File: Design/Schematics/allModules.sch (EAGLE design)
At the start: 188 parts, among them IC1 MAX7219CNG, IC2 MAX7219CNG, IC3 MAX7219CNG, IC4 MAX7219CNG, SW1 arcade_btn, SW2 arcade_btn, SW3 arcade_btn, SW4 arcade_btn, U1 328P, U2 328P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

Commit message: Updated memory schematic to I2C
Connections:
- new net PB5: R37.1, U6.PB5(SCK)
- new net SCL: U6.PC5(ADC5/SCL)
- new net SDA: U6.PC4(ADC4/SDA)
- net N$114: now also U6.PC3(ADC3); no longer R37.1, U6.PC2(ADC2), U6.PC4(ADC4/SDA)
- net N$134: now also U6.PC2(ADC2); no longer U6.PC3(ADC3)
- net NICS_RX: no longer U6.PB0(ICP)
- net NICS_TX: no longer U6.PB1(OC1A)
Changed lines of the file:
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@@
 <net name="N$114" class="0">
 <segment>
-<wire x1="-45.72" y1="-48.26" x2="-45.72" y2="-10.16" width="0.1524" layer="91"/>
+<wire x1="-45.72" y1="-48.26" x2="-45.72" y2="-12.7" width="0.1524" layer="91"/>
 <pinref part="R38" gate="G$1" pin="1"/>
-<pinref part="U6" gate="G$1" pin="PC4(ADC4/SDA)"/>
-<wire x1="-58.42" y1="-10.16" x2="-45.72" y2="-10.16" width="0.1524" layer="91"/>
-</segment>
-<segment>
-<wire x1="-53.34" y1="-40.64" x2="-53.34" y2="-17.78" width="0.1524" layer="91"/>
+<pinref part="U6" gate="G$1" pin="PC3(ADC3)"/>
+<wire x1="-45.72" y1="-12.7" x2="-58.42" y2="-12.7" width="0.1524" layer="91"/>
+</segment>
+<segment>
+<wire x1="-53.34" y1="-40.64" x2="-53.34" y2="-20.32" width="0.1524" layer="91"/>
 <wire x1="-53.34" y1="-40.64" x2="-76.2" y2="-40.64" width="0.1524" layer="91"/>
 <wire x1="-76.2" y1="-40.64" x2="-76.2" y2="-48.26" width="0.1524" layer="91"/>
 <pinref part="R36" gate="G$1" pin="1"/>
-<pinref part="U6" gate="G$1" pin="PC1(ADC1)"/>
-<wire x1="-53.34" y1="-17.78" x2="-58.42" y2="-17.78" width="0.1524" layer="91"/>
-</segment>
-<segment>
-<wire x1="-55.88" y1="-38.1" x2="-55.88" y2="-20.32" width="0.1524" layer="91"/>
-<wire x1="-88.9" y1="-38.1" x2="-55.88" y2="-38.1" width="0.1524" layer="91"/>
-<wire x1="-88.9" y1="-48.26" x2="-88.9" y2="-38.1" width="0.1524" layer="91"/>
-<pinref part="R37" gate="G$1" pin="1"/>
 <pinref part="U6" gate="G$1" pin="PC0(ADC0)"/>
-<wire x1="-58.42" y1="-20.32" x2="-55.88" y2="-20.32" width="0.1524" layer="91"/>
+<wire x1="-58.42" y1="-20.32" x2="-53.34" y2="-20.32" width="0.1524" layer="91"/>
 </segment>
 <segment>
 <wire x1="-66.04" y1="-48.26" x2="-66.04" y2="-43.18" width="0.1524" layer="91"/>
 <wire x1="-66.04" y1="-43.18" x2="-50.8" y2="-43.18" width="0.1524" layer="91"/>
-<wire x1="-50.8" y1="-43.18" x2="-50.8" y2="-15.24" width="0.1524" layer="91"/>
+<wire x1="-50.8" y1="-43.18" x2="-50.8" y2="-17.78" width="0.1524" layer="91"/>
 <pinref part="R35" gate="G$1" pin="1"/>
-<pinref part="U6" gate="G$1" pin="PC2(ADC2)"/>
-<wire x1="-58.42" y1="-15.24" x2="-50.8" y2="-15.24" width="0.1524" layer="91"/>
+<pinref part="U6" gate="G$1" pin="PC1(ADC1)"/>
+<wire x1="-50.8" y1="-17.78" x2="-58.42" y2="-17.78" width="0.1524" layer="91"/>
 </segment>
 </net>
@@
 <net name="N$134" class="0">
 <segment>
-<wire x1="-48.26" y1="-45.72" x2="-48.26" y2="-12.7" width="0.1524" layer="91"/>
+<wire x1="-48.26" y1="-45.72" x2="-48.26" y2="-15.24" width="0.1524" layer="91"/>
 <wire x1="-48.26" y1="-45.72" x2="-55.88" y2="-45.72" width="0.1524" layer="91"/>
 <wire x1="-55.88" y1="-45.72" x2="-55.88" y2="-48.26" width="0.1524" layer="91"/>
 <pinref part="R34" gate="G$1" pin="1"/>
-<pinref part="U6" gate="G$1" pin="PC3(ADC3)"/>
-<wire x1="-48.26" y1="-12.7" x2="-58.42" y2="-12.7" width="0.1524" layer="91"/>
+<pinref part="U6" gate="G$1" pin="PC2(ADC2)"/>
+<wire x1="-58.42" y1="-15.24" x2="-48.26" y2="-15.24" width="0.1524" layer="91"/>
 </segment>
 </net>
@@
 </segment>
 </net>
-<net name="NICS_RX" class="0">
-<segment>
-<pinref part="U6" gate="G$1" pin="PB0(ICP)"/>
-<wire x1="-58.42" y1="25.4" x2="-55.88" y2="25.4" width="0.1524" layer="91"/>
-<label x="-55.88" y="25.4" size="1.778" layer="95" rot="MR180"/>
-</segment>
-</net>
-<net name="NICS_TX" class="0">
-<segment>
-<pinref part="U6" gate="G$1" pin="PB1(OC1A)"/>
-<wire x1="-58.42" y1="27.94" x2="-48.26" y2="27.94" width="0.1524" layer="91"/>
-<label x="-48.26" y="27.94" size="1.778" layer="95" rot="MR180"/>
-</segment>
-</net>
 <net name="MEM_RX" class="0">
 <segment>
 <pinref part="U6" gate="G$1" pin="PD0(RXD)"/>
-<wire x1="-58.42" y1="2.54" x2="-53.34" y2="2.54" width="0.1524" layer="91"/>
-<label x="-53.34" y="2.54" size="1.778" layer="95" rot="MR270"/>
+<wire x1="-58.42" y1="2.54" x2="-48.26" y2="2.54" width="0.1524" layer="91"/>
+<label x="-48.26" y="2.54" size="1.778" layer="95" rot="R270"/>
 </segment>
 <segment>
@@
 <pinref part="U6" gate="G$1" pin="PD1(TXD)"/>
 <wire x1="-58.42" y1="5.08" x2="-45.72" y2="5.08" width="0.1524" layer="91"/>
-<label x="-45.72" y="5.08" size="1.778" layer="95" rot="MR270"/>
+<label x="-45.72" y="5.08" size="1.778" layer="95" rot="R270"/>
 </segment>
 <segment>
@@
 </segment>
 </net>
+<net name="PB5" class="0">
+<segment>
+<pinref part="U6" gate="G$1" pin="PB5(SCK)"/>
+<wire x1="-58.42" y1="38.1" x2="-55.88" y2="38.1" width="0.1524" layer="91"/>
+<label x="-55.88" y="38.1" size="1.778" layer="95"/>
+</segment>
+<segment>
+<wire x1="-88.9" y1="-48.26" x2="-88.9" y2="-38.1" width="0.1524" layer="91"/>
+<pinref part="R37" gate="G$1" pin="1"/>
+<label x="-88.9" y="-38.1" size="1.778" layer="95"/>
+</segment>
+</net>
+<net name="SCL" class="0">
+<segment>
+<pinref part="U6" gate="G$1" pin="PC5(ADC5/SCL)"/>
+<wire x1="-58.42" y1="-7.62" x2="-55.88" y2="-7.62" width="0.1524" layer="91"/>
+<label x="-55.88" y="-7.62" size="1.778" layer="95" rot="MR180"/>
+</segment>
+</net>
+<net name="SDA" class="0">
+<segment>
+<pinref part="U6" gate="G$1" pin="PC4(ADC4/SDA)"/>
+<wire x1="-58.42" y1="-10.16" x2="-53.34" y2="-10.16" width="0.1524" layer="91"/>
+<label x="-53.34" y="-10.16" size="1.778" layer="95" rot="MR180"/>
+</segment>
+</net>

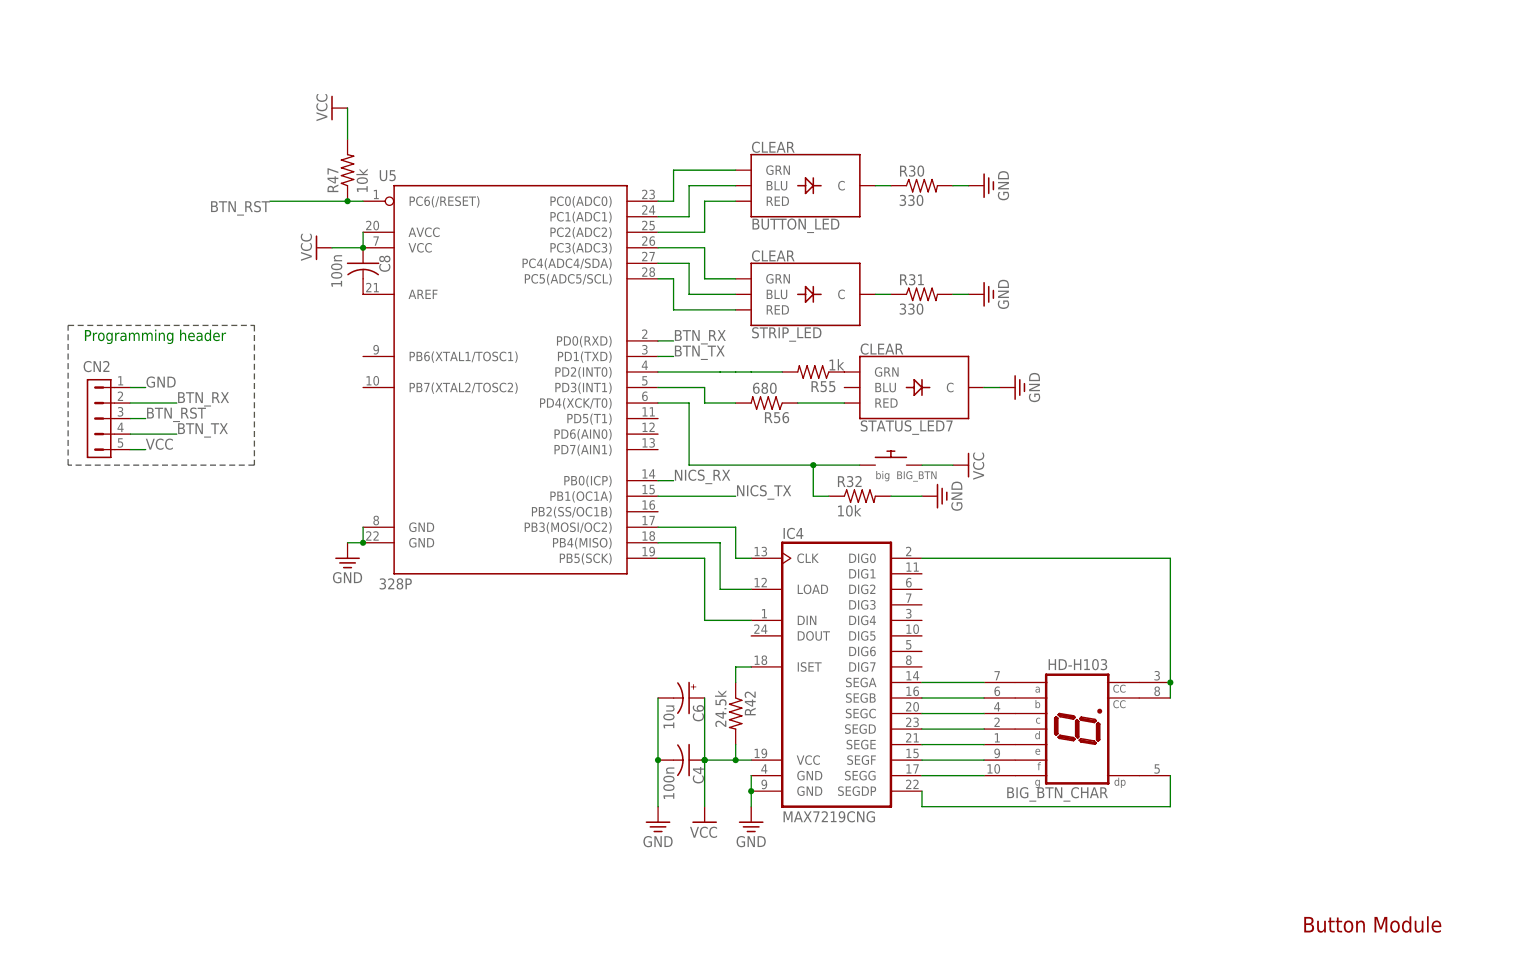
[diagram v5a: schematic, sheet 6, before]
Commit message: Updated modules for I2C and added external ADC for wires module
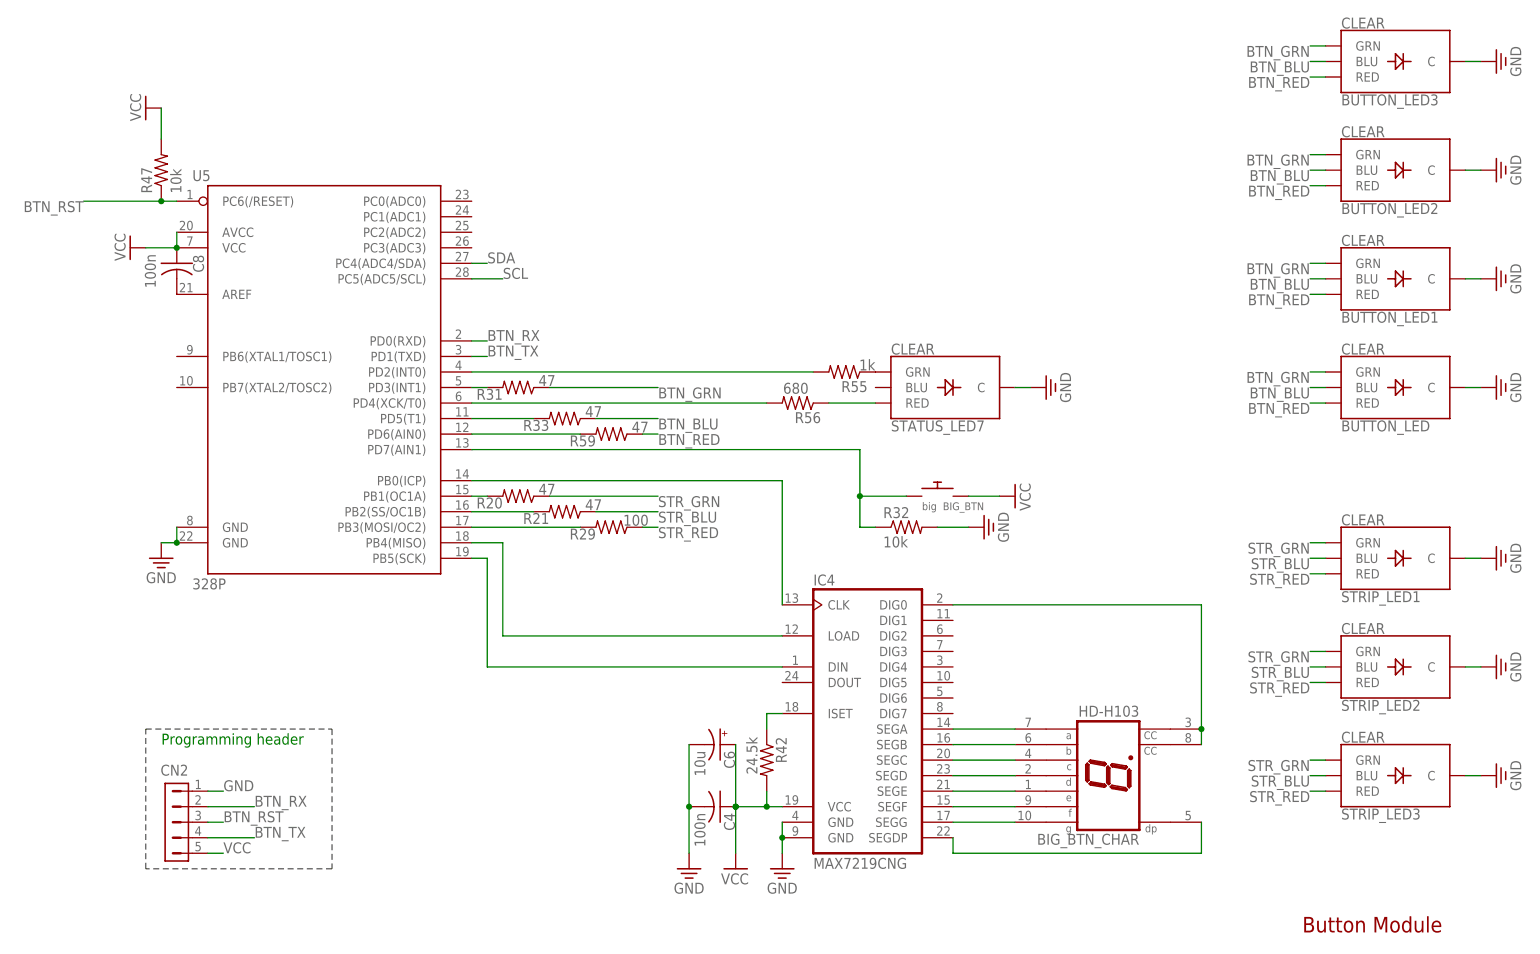
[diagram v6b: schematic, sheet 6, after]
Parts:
- removed CN7: (no value), con-hdrs40:HDR-1X2-MTA-100
- removed R30: 330, adafruit:R-US_0309/12
- removed S2: (no value), switch:320-938
- removed STRIP_LED: CLEAR, SparkFun-LED:LED-RGB-CCCLEAR
- added BUTTON_LED1, BUTTON_LED2, BUTTON_LED3, STRIP_LED1, STRIP_LED2, STRIP_LED3: CLEAR, SparkFun-LED:LED-RGB-CCCLEAR
- added IC5: MCP3008, adafruit:MCP3008
- added R20, R21, R33, R59: 47, adafruit:FLIPFLOP-RES
- added R29: 100, adafruit:FLIPFLOP-RES
- R31: value 330 -> 47; device adafruit:R-US_0309/12 -> adafruit:FLIPFLOP-RES
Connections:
- removed net DBG_RX: CN7.2, U1.PC0(ADC0)
- removed net DBG_TX: CN7.1, U1.PC1(ADC1)
- removed net MEGA_RX: S21.P, U1.PD0(RXD)
- removed net MEGA_TX: S2B.P, U1.PD1(TXD)
- removed net N$108: IC4.CLK, U5.PB3(MOSI/OC2)
- removed net N$127: STRIP_LED.BLU, U5.PC4(ADC4/SDA)
- removed net N$128: STRIP_LED.RED, U5.PC5(ADC5/SCL)
- removed net N$143: CN8.2, S21.S
- removed net N$80 (its old number): BUTTON_LED.C, R30.1
- new net BTN_BLU: BUTTON_LED.BLU, BUTTON_LED1.BLU, BUTTON_LED2.BLU, BUTTON_LED3.BLU, R33.1
- new net BTN_GRN: BUTTON_LED.GRN, BUTTON_LED1.GRN, BUTTON_LED2.GRN, BUTTON_LED3.GRN, R31.1
- new net BTN_RED: BUTTON_LED.RED, BUTTON_LED1.RED, BUTTON_LED2.RED, BUTTON_LED3.RED, R59.1
- new net MAIN_RX: CN8.2, U1.PD0(RXD)
- new net MAIN_TX: CN8.4, U1.PD1(TXD)
- new net N$69: R21.2, U5.PB2(SS/OC1B)
- new net N$72: R29.2, U5.PB3(MOSI/OC2)
- new net N$77: R31.2, U5.PD3(INT1)
- new net N$78: R33.2, U5.PD5(T1)
- new net N$90: IC5./CS, U4.PD7(AIN1)
- new net STR_BLU: R21.1, STRIP_LED1.BLU, STRIP_LED2.BLU, STRIP_LED3.BLU
- new net STR_GRN: R20.1, STRIP_LED1.GRN, STRIP_LED2.GRN, STRIP_LED3.GRN
- new net STR_RED: R29.1, STRIP_LED1.RED, STRIP_LED2.RED, STRIP_LED3.RED
- net ESP_RX: no longer S2B.O
- net ESP_TX: no longer S21.O
- net GND: now also BUTTON_LED.C, BUTTON_LED1.C, BUTTON_LED2.C, BUTTON_LED3.C, STRIP_LED1.C, STRIP_LED2.C, STRIP_LED3.C; no longer R30.2, R31.2
- net N$17: now also R20.2, U5.PB1(OC1A); no longer CN8.4, S2B.S
- net N$20: now also IC5.CH0; no longer U4.PC5(ADC5/SCL)
- net N$27: now also IC5.CH5; no longer U4.PC0(ADC0)
- net N$37: now also IC5.CH4; no longer U4.PC1(ADC1)
- net N$51: now also IC5.CH3; no longer U4.PC2(ADC2)
- net N$66: now also IC5.CH2; no longer U4.PC3(ADC3)
- net N$74: now also IC5.CH1; no longer U4.PC4(ADC4/SDA)
- net N$79: now also R59.2, U5.PD6(AIN0); no longer R56.2, U5.PD3(INT1)
- net N$81: now also U5.PD7(AIN1); no longer U5.PD4(XCK/T0)
- net N$83: now also R56.2, U5.PD4(XCK/T0); no longer R31.1, STRIP_LED.C
- net N$85: now also IC4.CLK, U5.PB0(ICP); no longer BUTTON_LED.GRN, U5.PC0(ADC0)
- net N$86: now also IC5.CLK, U4.PD4(XCK/T0); no longer BUTTON_LED.BLU, U5.PC1(ADC1)
- net N$87: now also IC5.DOUT, U4.PD5(T1); no longer BUTTON_LED.RED, U5.PC2(ADC2)
- net N$88: now also IC5.DIN, U4.PD6(AIN0); no longer STRIP_LED.GRN, U5.PC3(ADC3)
- net NICS_RX: no longer U1.PB0(ICP), U2.PB0(ICP), U5.PB0(ICP)
- net NICS_TX: no longer U1.PB1(OC1A), U2.PB1(OC1A), U5.PB1(OC1A)
- net SCL: now also U1.PC5(ADC5/SCL), U2.PC5(ADC5/SCL), U3.PC5(ADC5/SCL), U5.PC5(ADC5/SCL)
- net SDA: now also U1.PC4(ADC4/SDA), U2.PC4(ADC4/SDA), U3.PC4(ADC4/SDA), U5.PC4(ADC4/SDA)
- net SERIAL_CLK: now also U1.PC2(ADC2); no longer U1.PC4(ADC4/SDA)
- net SERIAL_CS: now also U1.PC0(ADC0); no longer U1.PC2(ADC2)
- net SERIAL_DIN: now also U1.PC1(ADC1); no longer U1.PC3(ADC3)
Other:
- note removed: "Serial for debugging"
- moved on the sheet: BIG_BTN, BIG_BTN_CHAR, BUTTON_LED, C4, C6, C8, C9, CN2, CN3, IC4, JP1, JP10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

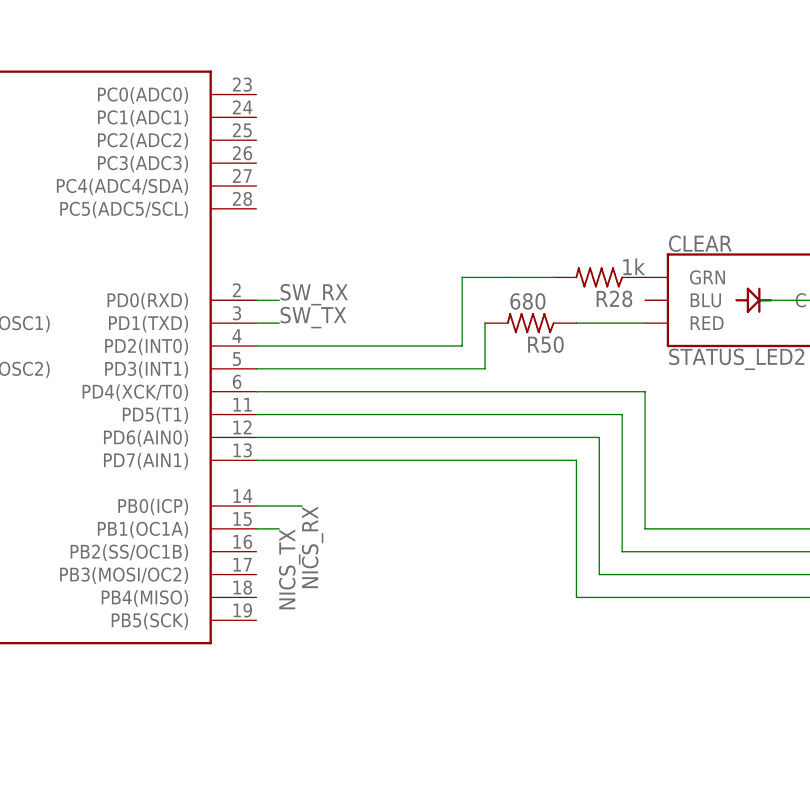
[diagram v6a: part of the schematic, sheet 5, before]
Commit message: Update all modules to use I2C
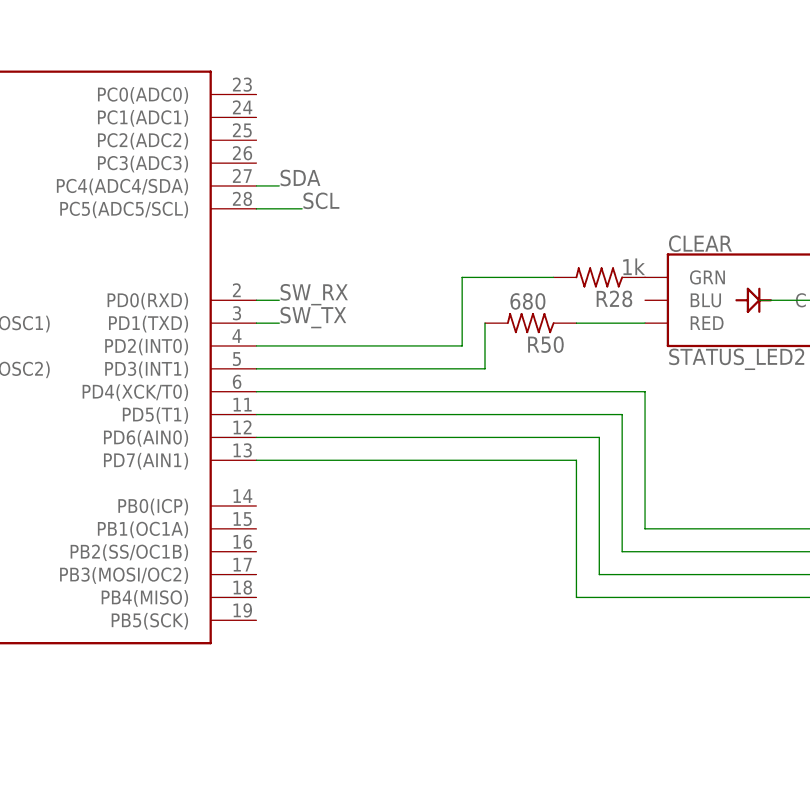
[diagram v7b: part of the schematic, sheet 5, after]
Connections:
- removed net NICS_RX: U3.PB0(ICP), U4.PB0(ICP)
- removed net NICS_TX: U3.PB1(OC1A), U4.PB1(OC1A)
- net SCL: now also U4.PC5(ADC5/SCL)
- net SDA: now also U4.PC4(ADC4/SDA)
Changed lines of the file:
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@@
-</segment>
-</net>
-<net name="NICS_RX" class="0">
-<segment>
-<pinref part="U3" gate="G$1" pin="PB0(ICP)"/>
-<wire x1="-48.26" y1="-17.78" x2="-45.72" y2="-17.78" width="0.1524" layer="91"/>
-<label x="-45.72" y="-17.78" size="1.778" layer="95"/>
-</segment>
-</net>
-<net name="NICS_TX" class="0">
-<segment>
-<pinref part="U3" gate="G$1" pin="PB1(OC1A)"/>
-<wire x1="-48.26" y1="-20.32" x2="-35.56" y2="-20.32" width="0.1524" layer="91"/>
-<label x="-35.56" y="-20.32" size="1.778" layer="95"/>
 </segment>
 </net>
@@
 <segment>
 <wire x1="-27.94" y1="15.24" x2="-27.94" y2="22.86" width="0.1524" layer="91"/>
-<wire x1="-27.94" y1="22.86" x2="-22.86" y2="22.86" width="0.1524" layer="91"/>
 <pinref part="U4" gate="G$1" pin="PD2(INT0)"/>
 <wire x1="-50.8" y1="15.24" x2="-27.94" y2="15.24" width="0.1524" layer="91"/>
 <pinref part="R28" gate="G$1" pin="2"/>
-<wire x1="-17.78" y1="22.86" x2="-22.86" y2="22.86" width="0.1524" layer="91"/>
+<wire x1="-17.78" y1="22.86" x2="-27.94" y2="22.86" width="0.1524" layer="91"/>
 </segment>
 </net>
@@
 <wire x1="-50.8" y1="12.7" x2="-25.4" y2="12.7" width="0.1524" layer="91"/>
 <pinref part="R50" gate="G$1" pin="2"/>
-</segment>
-</net>
-<net name="NICS_RX" class="0">
-<segment>
-<pinref part="U4" gate="G$1" pin="PB0(ICP)"/>
-<wire x1="-50.8" y1="-2.54" x2="-45.72" y2="-2.54" width="0.1524" layer="91"/>
-<label x="-45.72" y="-2.54" size="1.778" layer="95" rot="R270"/>
-</segment>
-</net>
-<net name="NICS_TX" class="0">
-<segment>
-<pinref part="U4" gate="G$1" pin="PB1(OC1A)"/>
-<wire x1="-50.8" y1="-5.08" x2="-48.26" y2="-5.08" width="0.1524" layer="91"/>
-<label x="-48.26" y="-5.08" size="1.778" layer="95" rot="R270"/>
 </segment>
 </net>
@@
 </segment>
 </net>
+<net name="SDA" class="0">
+<segment>
+<pinref part="U4" gate="G$1" pin="PC4(ADC4/SDA)"/>
+<wire x1="-50.8" y1="33.02" x2="-48.26" y2="33.02" width="0.1524" layer="91"/>
+<label x="-48.26" y="33.02" size="1.778" layer="95"/>
+</segment>
+</net>
+<net name="SCL" class="0">
+<segment>
+<pinref part="U4" gate="G$1" pin="PC5(ADC5/SCL)"/>
+<wire x1="-50.8" y1="30.48" x2="-45.72" y2="30.48" width="0.1524" layer="91"/>
+<label x="-45.72" y="30.48" size="1.778" layer="95"/>
+</segment>
+</net>
